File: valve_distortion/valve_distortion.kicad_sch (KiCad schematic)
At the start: 34 parts, among them J1 INPUT, J2 OUTPUT, J3 Conn_01x10, SW1 SW_ENABLE, U1 ECC83, U2 TL072

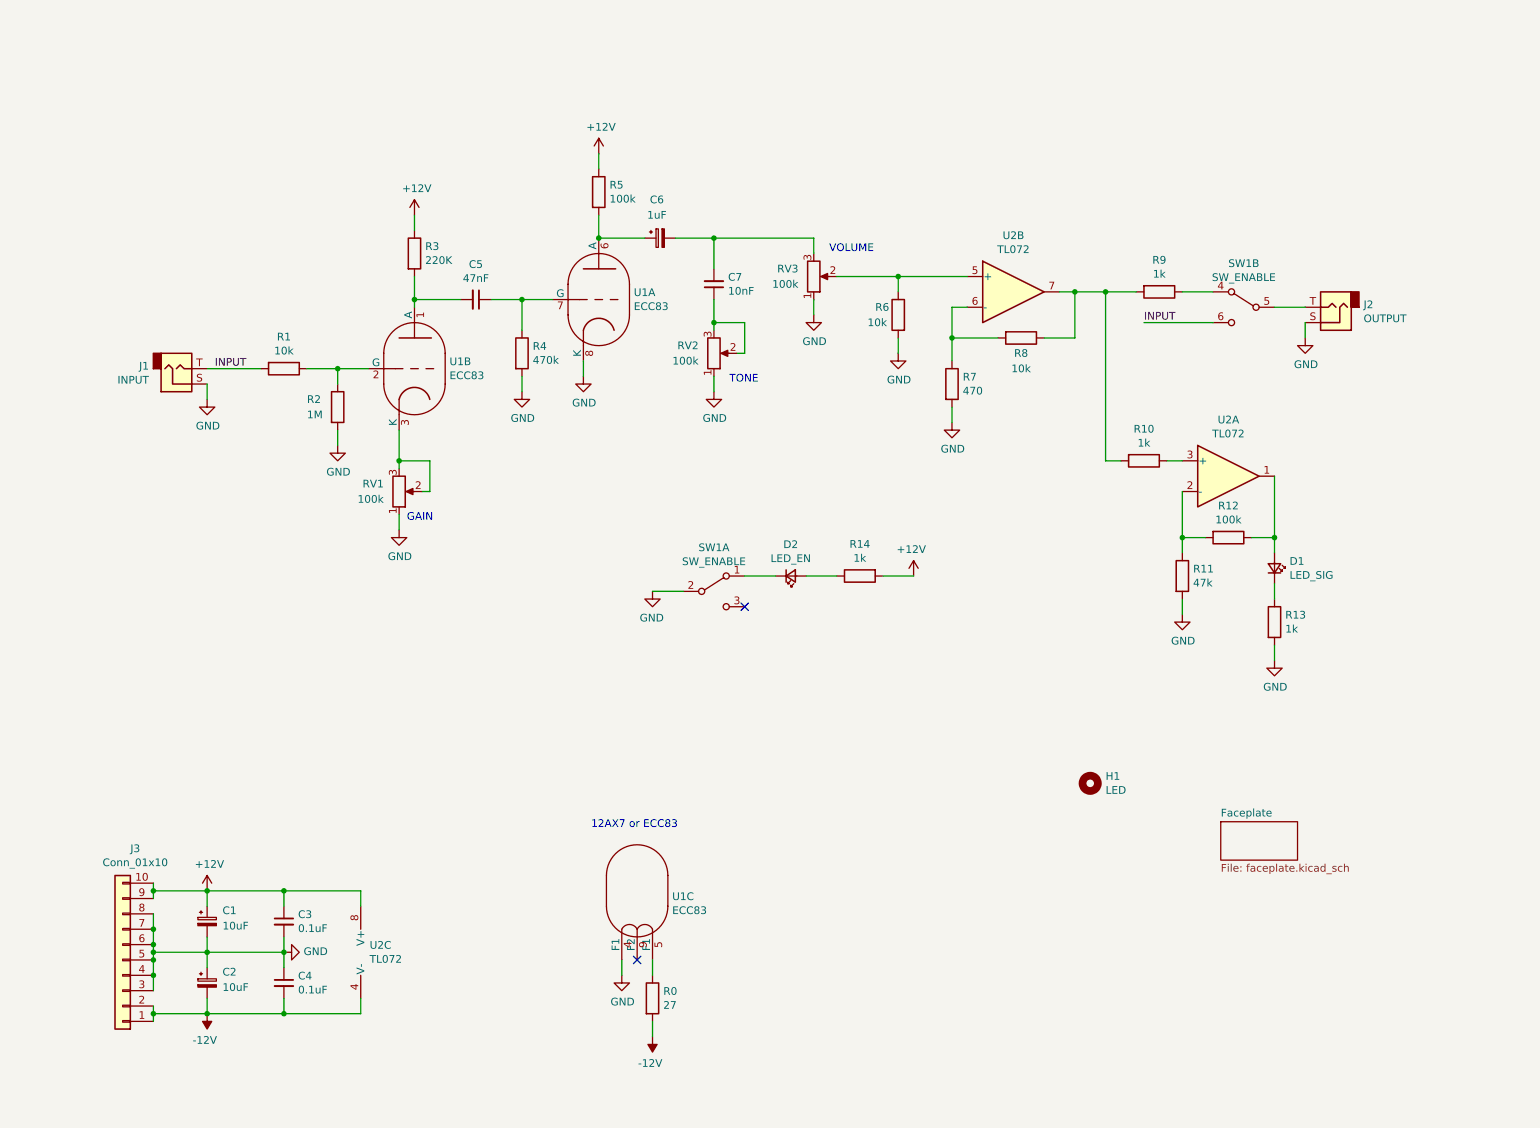
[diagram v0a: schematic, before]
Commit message: Add complete files for valve distortion euro module
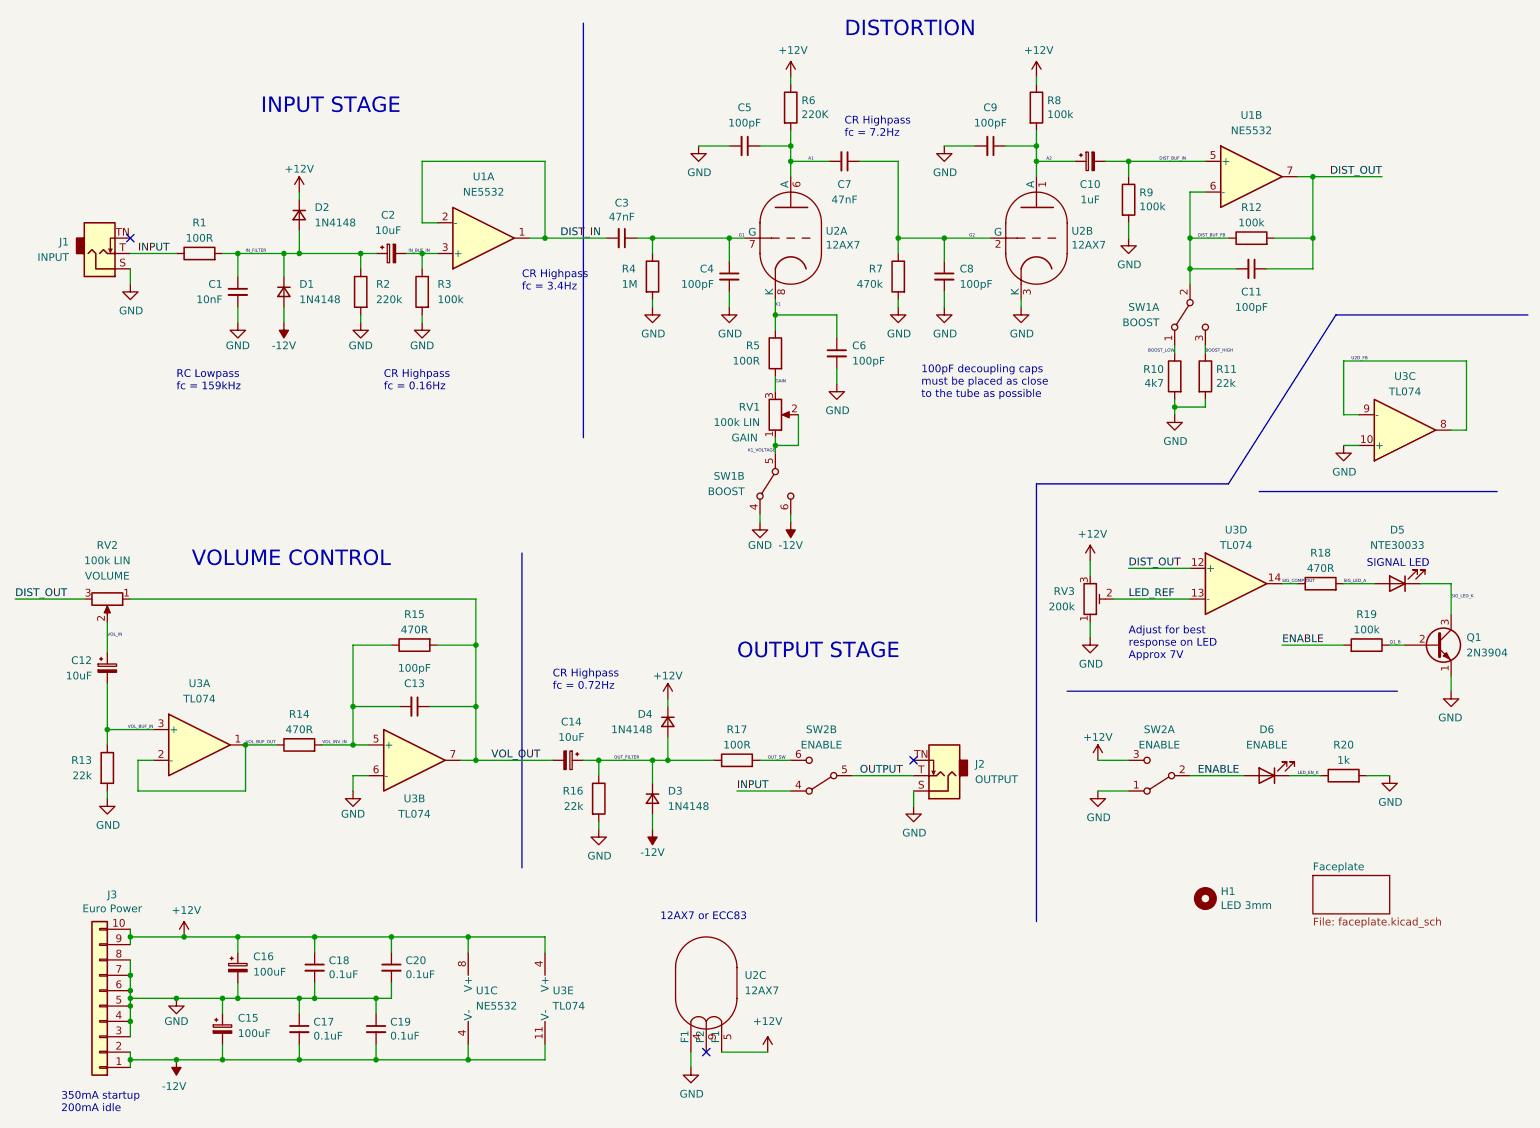
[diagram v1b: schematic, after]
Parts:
- removed C6: 1uF, Capacitor_THT:CP_Radial_D5.0mm_P2.50mm, symbol Device:C_Polarized_Small
- removed D1: LED_SIG, LED_THT:LED_D5.0mm, symbol Device:LED_Small
- removed D2: LED_EN, LED_THT:LED_D5.0mm, symbol Device:LED_Small
- removed J1: INPUT, Connector_Molex:Molex_KK-254_AE-6410-02A_1x02_P2.54mm_Vertical, symbol Connector:AudioJack2
- removed J2: OUTPUT, Connector_Molex:Molex_KK-254_AE-6410-02A_1x02_P2.54mm_Vertical, symbol Connector:AudioJack2
- removed R0: 27, Resistor_THT:R_Axial_DIN0207_L6.3mm_D2.5mm_P10.16mm_Horizontal, symbol Device:R
- removed RV3: 100k, Potentiometer_THT:Potentiometer_TT_P0915N, symbol Device:R_Potentiometer
- removed unit 1 of U1
- removed unit 2 of U1
- removed U2: TL072, Package_DIP:DIP-8_W7.62mm, symbol Amplifier_Operational:TL072
- added C1: 10nF, Capacitor_THT:C_Disc_D4.3mm_W1.9mm_P5.00mm, symbol Device:C_Small
- added C10: 1uF, Capacitor_THT:CP_Radial_D5.0mm_P2.50mm, symbol Device:C_Polarized_Small
- added C11, C13, C4, C6, C8, C9: 100pF, Capacitor_THT:C_Disc_D3.0mm_W1.6mm_P2.50mm, symbol Device:C_Small
- added C12, C14, C2: 10uF, Capacitor_THT:CP_Radial_D5.0mm_P2.50mm, symbol Device:C_Polarized_Small
- added C19, C20: 0.1uF, Capacitor_THT:C_Disc_D3.0mm_W1.6mm_P2.50mm, symbol Device:C_Small
- added C3: 47nF, Capacitor_THT:C_Disc_D3.0mm_W1.6mm_P2.50mm, symbol Device:C_Small
- added D1, D2, D3, D4: 1N4148, Diode_THT:D_DO-34_SOD68_P7.62mm_Horizontal, symbol Device:D_Small
- added D5: NTE30033, LED_THT:LED_D3.0mm_Clear, symbol Device:LED
- added D6: ENABLE, LED_THT:LED_D5.0mm, symbol Device:LED
- added J1: INPUT, kosmo-lib:Jack_3.5mm_QingPu_WQP-PJ301BM, symbol Connector:AudioJack2_SwitchT
- added J2: OUTPUT, kosmo-lib:Jack_3.5mm_QingPu_WQP-PJ301BM, symbol Connector:AudioJack2_SwitchT
- added Q1: 2N3904, Package_TO_SOT_THT:TO-92_Inline, symbol Transistor_BJT:2N3904
- added R15, R18: 470R, Resistor_THT:R_Axial_DIN0207_L6.3mm_D2.5mm_P10.16mm_Horizontal, symbol Device:R
- added R16: 22k, Resistor_THT:R_Axial_DIN0207_L6.3mm_D2.5mm_P10.16mm_Horizontal, symbol Device:R
- added R17: 100R, Resistor_THT:R_Axial_DIN0207_L6.3mm_D2.5mm_P10.16mm_Horizontal, symbol Device:R
- added R19: 100k, Resistor_THT:R_Axial_DIN0207_L6.3mm_D2.5mm_P10.16mm_Horizontal, symbol Device:R
- added R20: 1k, Resistor_THT:R_Axial_DIN0207_L6.3mm_D2.5mm_P10.16mm_Horizontal, symbol Device:R
- added RV3: 200k, kosmo-lib:Potentiometer_Trim_Horizontal, symbol Device:R_Potentiometer_Trim
- added unit 2 of SW1
- added unit 1 of SW2
- added U1: NE5532, Package_DIP:DIP-8_W7.62mm, symbol Amplifier_Operational:NE5532
- added unit 1 of U2
- added unit 2 of U2
- added U3: TL074, Package_DIP:DIP-14_W7.62mm, symbol Amplifier_Operational:TL074
- C15: renamed from C2; value 10uF -> 100uF
- C16: renamed from C1; value 10uF -> 100uF
- C5: value 47nF -> 100pF
- C7: value 10nF -> 47nF
- H1: value LED -> LED 3mm; footprint kosmo-lib:Hole_LED_5mm -> kosmo-lib:Hole_LED_3mm
- J3: value Conn_01x10 -> Euro Power
- R1: value 10k -> 100R
- R10: value 1k -> 4k7
- R11: value 47k -> 22k
- R13: value 1k -> 22k
- R14: value 1k -> 470R
- R2: value 1M -> 220k
- R3: value 220K -> 100k
- R4: value 470k -> 1M
- R5: value 100k -> 100R
- R6: value 10k -> 220K
- R7: value 470 -> 470k
- R8: value 10k -> 100k
- R9: value 1k -> 100k
- RV1: value 100k -> 100k LIN; Function (none) -> GAIN
- RV2: value 100k -> 100k LIN; Function (none) -> VOLUME
- SW1: value SW_ENABLE -> BOOST; footprint kosmo-lib:GR5-326-XXXX -> kosmo-lib:Switch_DPDT
- SW2: renamed from SW1; value SW_ENABLE -> ENABLE; footprint kosmo-lib:GR5-326-XXXX -> kosmo-lib:Switch_DPDT
- U2: renamed from U1; value ECC83 -> 12AX7
- renumbered C4 to C17, C3 to C18
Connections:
- net +12V: now also R6.1, R8.1, U2.5 (F1), C20.1, D2.1 (K), D4.1 (K), RV3.3, SW2.3 (C), U1.8 (V+), U3.4 (V+); no longer R14.2, R3.1, R5.1
- net -12V: now also C19.2, D1.2 (A), D3.2 (A), SW1.6 (C), U1.4 (V-), U3.11 (V-)
- net GND: now also C5.2, R10.2, R3.2, R9.2, C1.2, C19.1, C20.2, C4.2, C6.2, C8.2, C9.2, J1.S, J2.S, Q1.1 (E), R16.2, R20.2, RV3.1, SW1.4 (A), SW2.1 (A), U2.3 (K), U3.10 (+), U3.6 (-); no longer R6.2, RV1.1, RV2.1, SW1.2 (B)
- net INPUT: now also R1.1, SW2.4 (A), J1.T; no longer R1.2, SW2.6 (C)
- net GAIN: now reaches R5.2
- net GAIN: now also RV1.3
- net A1: now reaches C5.1
- net A1: now also C7.2, R6.2, U2.6 (A); no longer R4.1
- net IN_FILTER: now reaches R2.1
- net IN_FILTER: now also R1.2, C1.1, C2.1, D1.1 (K), D2.2 (A); no longer R1.1
- net K1_VOLTAGE: now reaches RV1.2
- net K1_VOLTAGE: now also RV1.1, SW1.5 (B); no longer RV1.3
- net OUTPUT: now reaches SW2.5 (B)
- net OUTPUT: now also J2.T
- net A2: now reaches R8.2
- net A2: now also C10.1, C9.1, U2.1 (A); no longer R7.1
- net DIST_BUF_FB: now reaches R12.1
- net DIST_BUF_FB: now also SW1.2 (B), C11.2, U1.6 (-)
- net BOOST_HIGH: now reaches R11.1
- net BOOST_HIGH: now also SW1.3 (C); no longer R12.2
- net BOOST_LOW: now reaches R10.1
- net BOOST_LOW: now also SW1.1 (A)
- net DIST_BUF_IN: now reaches R9.1
- net DIST_BUF_IN: now also C10.2, U1.5 (+); no longer SW2.4 (A)
- net VOL_BUF_IN: now reaches R13.1
- net VOL_BUF_IN: now also C12.2, U3.3 (+)
- net VOL_BUF_OUT: now reaches R14.1
- net VOL_BUF_OUT: now also U3.1, U3.2 (-)
- new net DIST_IN: C3.2, U1.1, U1.2 (-)
- new net DIST_OUT: C11.1, R12.2, RV2.3, U1.7, U3.12 (+)
- new net ENABLE: D6.2 (A), R19.2, SW2.2 (B)
- new net G1: C3.1, C4.1, R4.1, U2.7 (G)
- new net G2: C7.1, C8.1, R7.1, U2.2 (G)
- new net IN_BUF_IN: C2.2, R3.1, U1.3 (+)
- new net K1: C6.1, R5.1, U2.8 (K)
- new net LED_EN_K: D6.1 (K), R20.1
- new net LED_REF: RV3.2, U3.13 (-)
- new net OUT_FILTER: C14.1, D3.1 (K), D4.2 (A), R16.1, R17.1
- new net OUT_SW: R17.2, SW2.6 (C)
- new net Q1_B: Q1.2 (B), R19.1
- new net SIG_COMP_OUT: R18.1, U3.14
- new net SIG_LED_A: D5.2 (A), R18.2
- new net SIG_LED_K: D5.1 (K), Q1.3 (C)
- new net U2D_FB: U3.8, U3.9 (-)
- new net VOL_IN: C12.1, RV2.2
- new net VOL_INV_IN: C13.2, R14.2, R15.1, U3.5 (+)
- new net VOL_OUT: C13.1, C14.2, R15.2, RV2.1, U3.7
- no-connect marks 2 -> 3
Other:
- note added: "100pF decoupling caps must be placed as close to the tube as possible"
- note added: "350mA startup 200mA idle"
- note added: "Adjust for best response on LED Approx 7V"
- note added: "CR Highpass fc = 0.16Hz"
- note added: "CR Highpass fc = 0.72Hz"
- note added: "CR Highpass fc = 3.4Hz"
- note added: "CR Highpass fc = 7.2Hz"
- note added: "DISTORTION"
- note added: "INPUT STAGE"
- note added: "OUTPUT STAGE"
- note added: "RC Lowpass fc = 159kHz"
- note added: "SIGNAL LED"
- note added: "VOLUME CONTROL"
- note removed: "GAIN"
- note removed: "TONE"
- note removed: "VOLUME"
- company: xperseai -> Max Proskauer
- title: Valve Distortion -> Valve Distortion Euro Module
- moved on the sheet: C15, C16, C17, C18, H1, J3, SW2B, U2C

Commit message: Fix rev1 pcb issues
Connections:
- net GND: now also J1.TN
- no-connect marks 3 -> 2
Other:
- moved on the sheet: J1
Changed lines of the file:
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@@
   (junction (at 35.56 181.61) (diameter 0) (color 0 0 0 0)
+  )
+  (junction (at 35.56 60.96) (diameter 0) (color 0 0 0 0)
   )
   (junction (at 91.44 191.77) (diameter 0) (color 0 0 0 0)
@@
   (no_connect (at 165.1 142.24))
   (no_connect (at 130.81 190.5))
-  (no_connect (at 35.56 55.88))
   (wire (pts (xy 104.14 191.77) (xy 91.44 191.77))
     (stroke (width 0) (type default) (color 0 0 0 0))
@@
     (stroke (width 0) (type default) (color 0 0 0 0))
   )
+  (wire (pts (xy 35.56 60.96) (xy 35.56 63.5))
+    (stroke (width 0) (type default) (color 0 0 0 0))
+  )
   (wire (pts (xy 139.7 142.24) (xy 144.78 142.24))
     (stroke (width 0) (type default) (color 0 0 0 0))
@@
     (stroke (width 0) (type default) (color 0 0 0 0))
   )
+  (wire (pts (xy 33.02 60.96) (xy 35.56 60.96))
+    (stroke (width 0) (type default) (color 0 0 0 0))
+  )
   (wire (pts (xy 83.82 68.58) (xy 83.82 69.85))
     (stroke (width 0) (type default) (color 0 0 0 0))
@@
     (stroke (width 0) (type default) (color 0 0 0 0))
   )
+  (wire (pts (xy 35.56 60.96) (xy 35.56 55.88))
+    (stroke (width 0) (type default) (color 0 0 0 0))
+  )
   (wire (pts (xy 144.78 43.18) (xy 144.78 45.72))
     (stroke (width 0) (type default) (color 0 0 0 0))
@@
     (stroke (width 0) (type default) (color 0 0 0 0))
   )
-  (wire (pts (xy 35.56 60.96) (xy 35.56 63.5))
-    (stroke (width 0) (type default) (color 0 0 0 0))
-  )
   (wire (pts (xy 35.56 180.34) (xy 35.56 181.61))
     (stroke (width 0) (type default) (color 0 0 0 0))
@@
     (stroke (width 0) (type default) (color 0 0 0 0))
   )
-  (wire (pts (xy 35.56 58.42) (xy 43.18 58.42))
+  (wire (pts (xy 33.02 58.42) (xy 43.18 58.42))
     (stroke (width 0) (type default) (color 0 0 0 0))
   )
@@
   )
   (wire (pts (xy 170.18 40.64) (xy 175.26 40.64))
+    (stroke (width 0) (type default) (color 0 0 0 0))
+  )
+  (wire (pts (xy 35.56 55.88) (xy 33.02 55.88))
     (stroke (width 0) (type default) (color 0 0 0 0))
   )
@@
     (pin "1")
   )
-  (symbol (lib_id "Connector:AudioJack2_SwitchT") (at 30.48 58.42 0) (mirror x) (unit 1)
+  (symbol (lib_id "Connector:AudioJack2_SwitchT") (at 27.94 58.42 0) (mirror x) (unit 1)
     (in_bom yes) (on_board yes) (fields_autoplaced)
-    (property "Reference" "J1" (id 0) (at 25.4 56.5149 0)
+    (property "Reference" "J1" (id 0) (at 22.86 56.5149 0)
       (effects (font (size 1.27 1.27)) (justify right))
     )
-    (property "Value" "INPUT" (id 1) (at 25.4 59.0549 0)
+    (property "Value" "INPUT" (id 1) (at 22.86 59.0549 0)
       (effects (font (size 1.27 1.27)) (justify right))
     )
-    (property "Footprint" "kosmo-lib:Jack_3.5mm_QingPu_WQP-PJ301BM" (id 2) (at 30.48 58.42 0)
-      (effects (font (size 1.27 1.27)) hide)
-    )
-    (property "Datasheet" "~" (id 3) (at 30.48 58.42 0)
-      (effects (font (size 1.27 1.27)) hide)
-    )
+    (property "Footprint" "kosmo-lib:Jack_3.5mm_QingPu_WQP-PJ301BM" (id 2) (at 27.94 58.42 0)
+      (effects (font (size 1.27 1.27)) hide)
+    )
+    (property "Datasheet" "~" (id 3) (at 27.94 58.42 0)
+      (effects (font (size 1.27 1.27)) hide)
+    )
